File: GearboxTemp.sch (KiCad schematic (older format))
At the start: 4 parts

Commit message: Checkpoint before trying 4 layer
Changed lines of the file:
@@
 $Descr A4 11693 8268
 encoding utf-8
-Sheet 19 50
+Sheet 14 37
 Title ""
 Date ""
@@
 AR Path="/6049E76F/604A26D2" Ref="FL12"  Part="1"
 AR Path="/604A00E2/604A26D2" Ref="FL16"  Part="1"
-F 0 "FL16" H 5600 3965 50  0000 C CNN
+F 0 "FL12" H 5600 3965 50  0000 C CNN
 F 1 "DLP11SA900HL2L" H 5600 3874 50  0000 C CNN
 F 2 "SamacSys_Parts:DLP11SA350HL2B" H 5850 3800 50  0001 L CNN
@@
 AR Path="/6049E76F/604A26D3" Ref="R64"  Part="1"
 AR Path="/604A00E2/604A26D3" Ref="R72"  Part="1"
-F 0 "R72" V 6345 3400 50  0000 C CNN
+F 0 "R64" V 6345 3400 50  0000 C CNN
 F 1 "1K" V 6436 3400 50  0000 C CNN
 F 2 "Resistor_SMD:R_0805_2012Metric" V 6590 3390 50  0001 C CNN
@@
 AR Path="/6049E76F/604A26D4" Ref="R68"  Part="1"
 AR Path="/604A00E2/604A26D4" Ref="R76"  Part="1"
-F 0 "R76" V 6345 3700 50  0000 C CNN
+F 0 "R68" V 6345 3700 50  0000 C CNN
 F 1 "1K" V 6436 3700 50  0000 C CNN
 F 2 "Resistor_SMD:R_0805_2012Metric" V 6590 3690 50  0001 C CNN
@@
 AR Path="/6049E76F/604A26D5" Ref="C58"  Part="1"
 AR Path="/604A00E2/604A26D5" Ref="C62"  Part="1"
-F 0 "C62" H 7015 3996 50  0000 L CNN
+F 0 "C58" H 7015 3996 50  0000 L CNN
 F 1 "0.1uF" H 7015 3905 50  0000 L CNN
 F 2 "Capacitor_SMD:C_0805_2012Metric" H 6900 3950 50  0001 C CNN

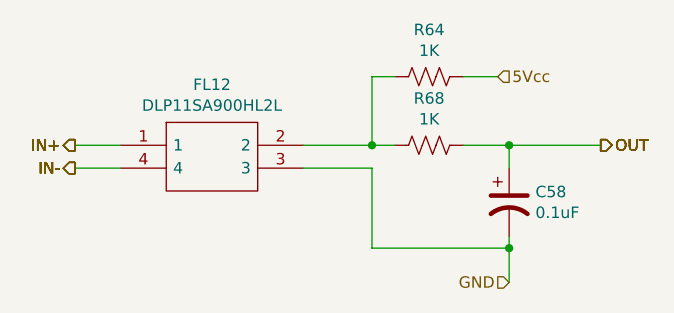
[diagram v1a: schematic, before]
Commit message: 4 layer board that passes checks
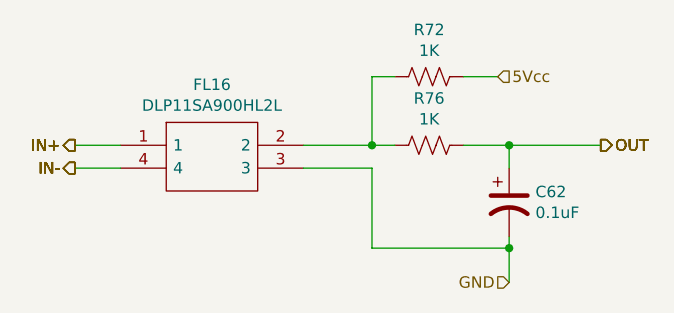
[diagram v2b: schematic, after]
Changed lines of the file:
@@
 $Descr A4 11693 8268
 encoding utf-8
-Sheet 14 37
+Sheet 15 36
 Title ""
 Date ""
@@
 AR Path="/6049E76F/604A26D2" Ref="FL12"  Part="1"
 AR Path="/604A00E2/604A26D2" Ref="FL16"  Part="1"
-F 0 "FL12" H 5600 3965 50  0000 C CNN
+F 0 "FL16" H 5600 3965 50  0000 C CNN
 F 1 "DLP11SA900HL2L" H 5600 3874 50  0000 C CNN
 F 2 "SamacSys_Parts:DLP11SA350HL2B" H 5850 3800 50  0001 L CNN
@@
 AR Path="/6049E76F/604A26D3" Ref="R64"  Part="1"
 AR Path="/604A00E2/604A26D3" Ref="R72"  Part="1"
-F 0 "R64" V 6345 3400 50  0000 C CNN
+F 0 "R72" V 6345 3400 50  0000 C CNN
 F 1 "1K" V 6436 3400 50  0000 C CNN
 F 2 "Resistor_SMD:R_0805_2012Metric" V 6590 3390 50  0001 C CNN
@@
 AR Path="/6049E76F/604A26D4" Ref="R68"  Part="1"
 AR Path="/604A00E2/604A26D4" Ref="R76"  Part="1"
-F 0 "R68" V 6345 3700 50  0000 C CNN
+F 0 "R76" V 6345 3700 50  0000 C CNN
 F 1 "1K" V 6436 3700 50  0000 C CNN
 F 2 "Resistor_SMD:R_0805_2012Metric" V 6590 3690 50  0001 C CNN
@@
 AR Path="/6049E76F/604A26D5" Ref="C58"  Part="1"
 AR Path="/604A00E2/604A26D5" Ref="C62"  Part="1"
-F 0 "C58" H 7015 3996 50  0000 L CNN
+F 0 "C62" H 7015 3996 50  0000 L CNN
 F 1 "0.1uF" H 7015 3905 50  0000 L CNN
 F 2 "Capacitor_SMD:C_0805_2012Metric" H 6900 3950 50  0001 C CNN

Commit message: Routed PCB
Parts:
- C50: JLCPCB_PN (none) -> C49678
- FL4: JLCPCB_PN (none) -> C76895
- R48, R52: JLCPCB_PN (none) -> C17513
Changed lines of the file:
@@
 F 8 "Murata Electronics" H 5850 3200 50  0001 L CNN "Manufacturer_Name"
 F 9 "DLP11SA900HL2L" H 5850 3100 50  0001 L CNN "Manufacturer_Part_Number"
+F 10 "C76895" H 5200 3700 50  0001 C CNN "JLCPCB_PN"
 	1    5200 3700
 	1    0    0    -1
@@
 F 2 "Resistor_SMD:R_0805_2012Metric" V 6590 3390 50  0001 C CNN
 F 3 "~" H 6550 3400 50  0001 C CNN
+F 4 "C17513" H 6550 3400 50  0001 C CNN "JLCPCB_PN"
 	1    6550 3400
 	0    1    1    0
@@
 F 2 "Resistor_SMD:R_0805_2012Metric" V 6590 3690 50  0001 C CNN
 F 3 "~" H 6550 3700 50  0001 C CNN
+F 4 "C17513" H 6550 3700 50  0001 C CNN "JLCPCB_PN"
 	1    6550 3700
 	0    1    1    0
@@
 F 2 "Capacitor_SMD:C_0805_2012Metric" H 6900 3950 50  0001 C CNN
 F 3 "~" H 6900 3950 50  0001 C CNN
+F 4 "C49678" H 6900 3950 50  0001 C CNN "JLCPCB_PN"
 	1    6900 3950
 	1    0    0    -1
